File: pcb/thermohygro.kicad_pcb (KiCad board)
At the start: 2 copper layers, 50.8 x 43.2 mm, 9 parts, among them J1 RJ45_Shielded, J2 RJ45_Shielded, J3 SSD1306, U1 XIAO-ESP32-S3

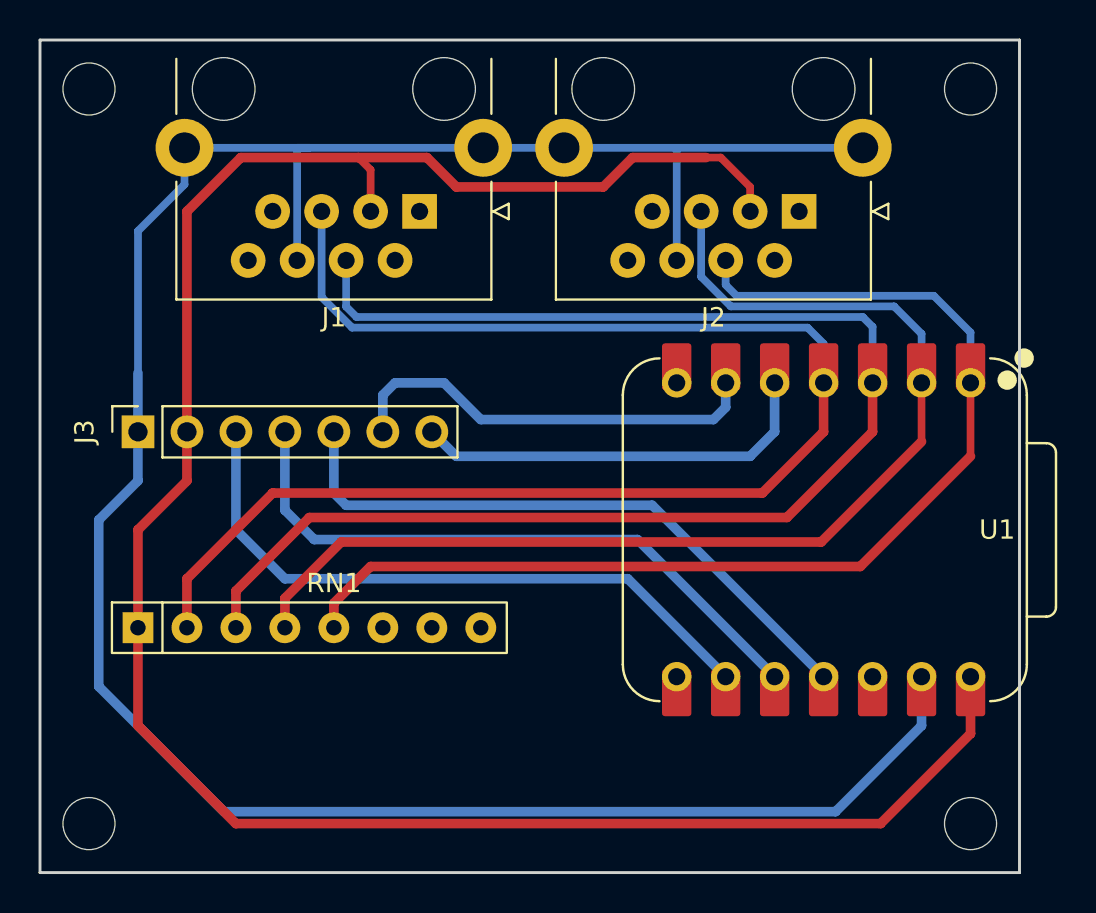
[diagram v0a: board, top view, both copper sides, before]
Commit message: closer RJ45
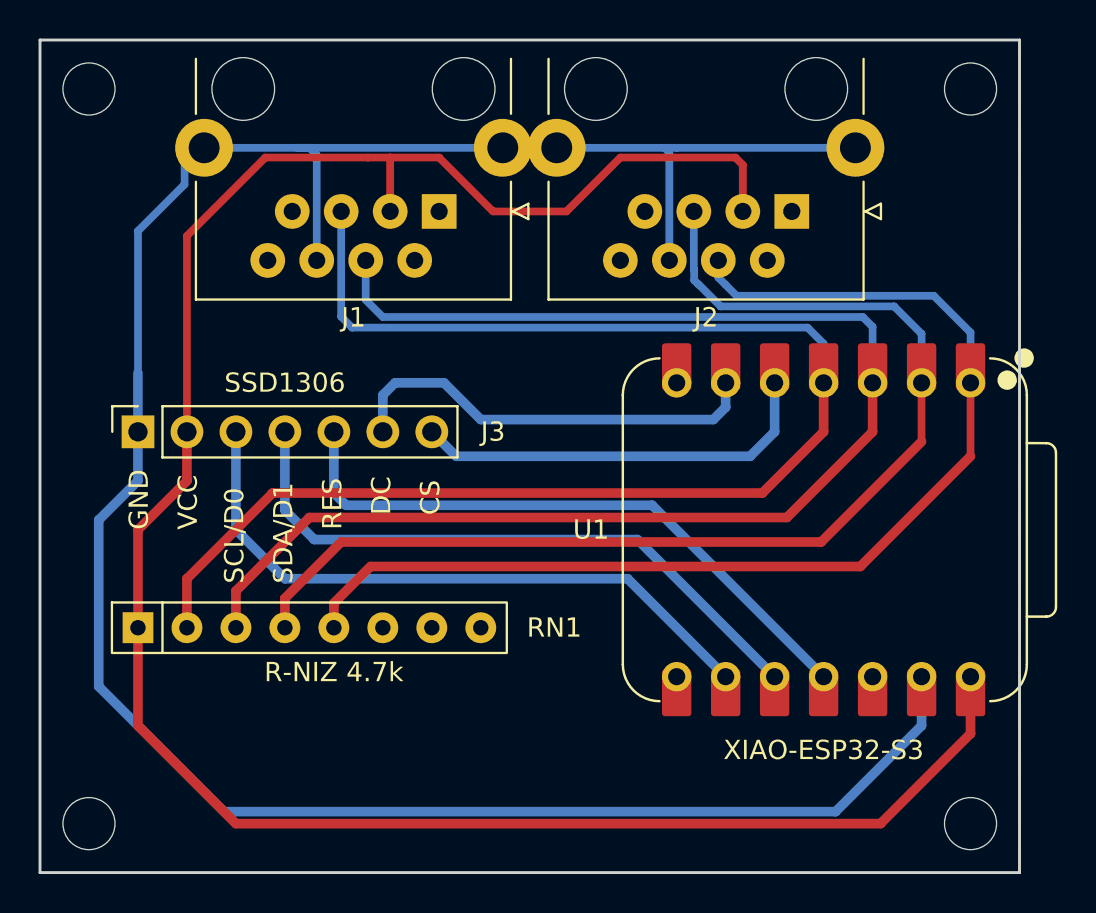
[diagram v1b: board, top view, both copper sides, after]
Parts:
- J1, J2: footprint Connector_RJ:RJ45_HALO_HFJ11-x2450HRL_Horizontal -> rj45:RJ45_HALO_HFJ11-x2450HRL_Horizontal_closer
- moved J1 1.02 mm to (75.7, 110.7)
- moved J2 0.38 mm to (94.0, 110.7)
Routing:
- net /SCK1: track 73.9 -> 72.7 mm
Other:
- rule pad_to_mask_clearance: 0 -> 0.08
- board text added: "CS"
- board text added: "DC"
- board text added: "GND"
- board text added: "RES"
- board text added: "SCL/D0"
- board text added: "SDA/D1"
- board text added: "VCC"
